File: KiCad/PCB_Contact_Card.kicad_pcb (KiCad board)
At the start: 2 copper layers, 90 x 54 mm, 6 parts

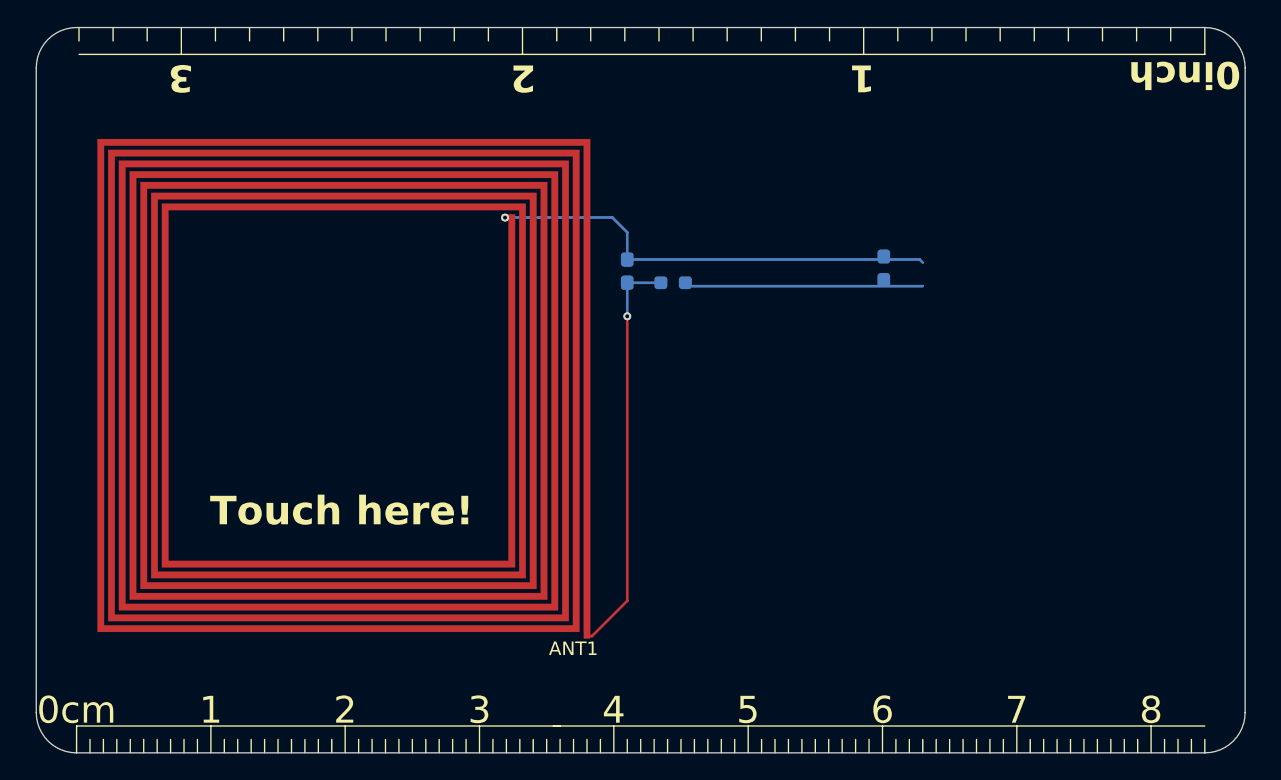
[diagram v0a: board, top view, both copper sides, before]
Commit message: footprint fixed
アンテナのフットプリントのバク修正
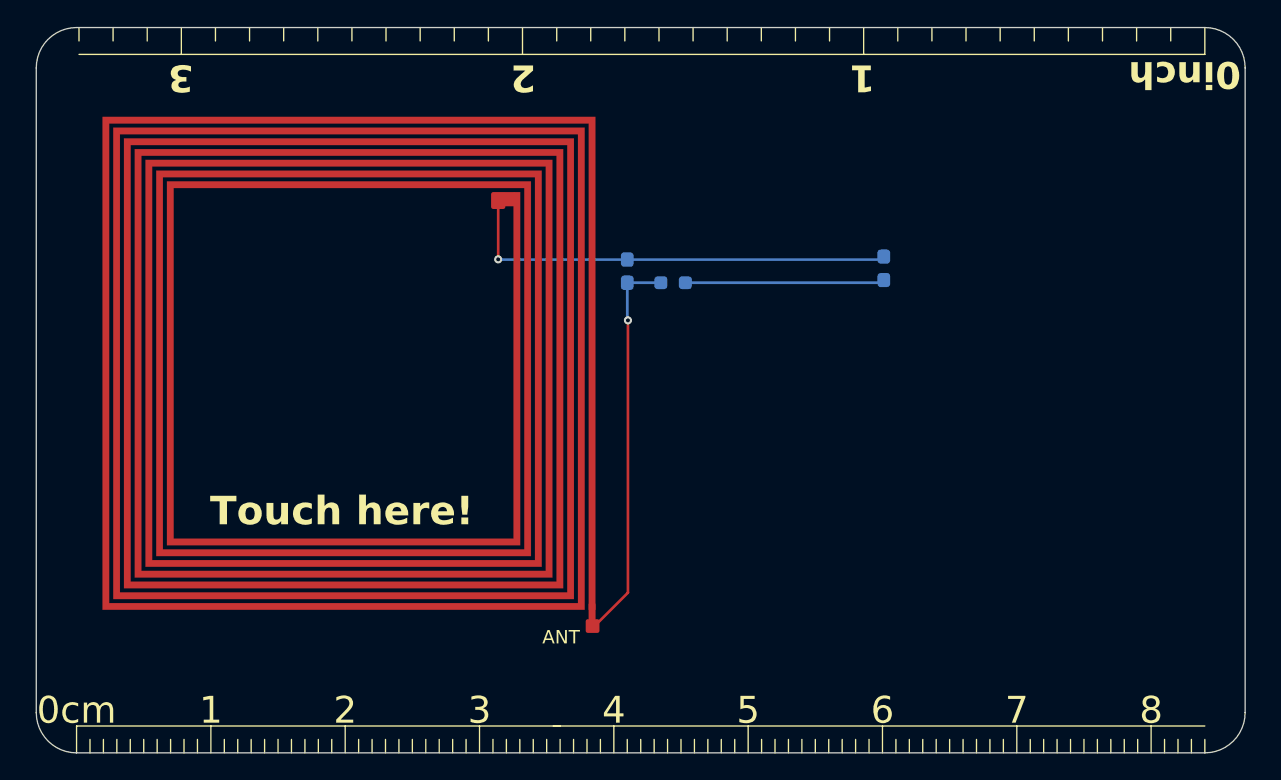
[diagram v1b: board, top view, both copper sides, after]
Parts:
- removed ANT1: L, PCB_BusinessCard_lib:NFC_COIL_36.7x36.7_3uH
- added ANT: L, lib:NFC_COIL_36.7x36.7_3uH, F.Cu at (116.6, 85.8)
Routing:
- net Net-(D1-A): track 17.8 -> 15.2 mm
- net Net-(C1-Pad2): track 30.3 -> 29.3 mm
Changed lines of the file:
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@@
 	(net 1 "Net-(D1-A)")
 	(net 2 "Net-(D1-K)")
-	(net 3 "Net-(ANT1-Pad1)")
-	(footprint "PCB_BusinessCard_lib:NFC_COIL_36.7x36.7_3uH"
+	(net 3 "Net-(C1-Pad2)")
+	(footprint "lib:NFC_COIL_36.7x36.7_3uH"
 		(layer "F.Cu")
-		(at 116.25 87.5 90)
-		(property "Reference" "ANT1"
-			(at -1.25 -1.25 0)
+		(at 116.63 85.85 90)
+		(property "Reference" "ANT"
+			(at -2.04 -2.56 0)
 			(unlocked yes)
 			(layer "F.SilkS")
@@
 		)
 		(property "Value" "L"
-			(at 0 1 90)
+			(at -0.07 1.55 90)
 			(unlocked yes)
 			(layer "F.Fab")
@@
 		(property ki_fp_filters "Choke_* *Coil* Inductor_* L_*")
 		(sheetname "/")
-		(sheetfile "PCB_BusinessCard.kicad_sch")
+		(sheetfile "PCB_Contact_Card.kicad_sch")
 		(attr smd)
+		(fp_rect
+			(start 30.14 -6.795)
+			(end 31 -6.105)
+			(stroke
+				(width 0.2)
+				(type solid)
+			)
+			(fill yes)
+			(layer "F.Cu")
+		)
+		(fp_rect
+			(start -0.67 -0.41)
+			(end 0.41 -0.09)
+			(stroke
+				(width 0.2)
+				(type solid)
+			)
+			(fill yes)
+			(layer "F.Cu")
+		)
 		(fp_poly
 			(pts
@@
 				(xy 2.4 -34.3) (xy 2.4 -3.2) (xy 33.5 -3.2) (xy 33.5 -33.5) (xy 3.2 -33.5) (xy 3.2 -4) (xy 32.7 -4)
 				(xy 32.7 -32.7) (xy 4 -32.7) (xy 4 -4.8) (xy 31.9 -4.8) (xy 31.9 -31.9) (xy 4.8 -31.9) (xy 4.8 -5.6)
-				(xy 31.1 -5.6) (xy 31.1 -6.1) (xy 30.6 -6.1) (xy 5.3 -6.1) (xy 5.3 -31.4) (xy 31.4 -31.4) (xy 31.4 -5.3)
+				(xy 31.1 -5.6) (xy 31.1 -6.1) (xy 30 -6.1) (xy 5.3 -6.1) (xy 5.3 -31.4) (xy 31.4 -31.4) (xy 31.4 -5.3)
 				(xy 4.5 -5.3) (xy 4.5 -32.2) (xy 32.2 -32.2) (xy 32.2 -4.5) (xy 3.7 -4.5) (xy 3.7 -33) (xy 33 -33)
 				(xy 33 -3.7) (xy 2.9 -3.7) (xy 2.9 -33.8) (xy 33.8 -33.8) (xy 33.8 -2.9) (xy 2.1 -2.9) (xy 2.1 -34.6)
@@
 			(layer "F.CrtYd")
 		)
-		(pad "1" smd rect
-			(at -0.25 -0.25 90)
-			(size 0.5 0.5)
+		(pad "1" smd roundrect
+			(at 30.470625 -7.23875 90)
+			(size 1.26125 1.0625)
 			(layers "F.Cu" "F.Mask" "F.Paste")
-			(net 3 "Net-(ANT1-Pad1)")
+			(roundrect_rratio 0.15)
+			(net 2 "Net-(D1-K)")
 			(pinfunction "1")
 			(pintype "passive")
-			(thermal_bridge_angle 45)
 		)
-		(pad "2" smd rect
-			(at 30.85 -6.35 90)
-			(size 0.5 0.5)
+		(pad "2" smd roundrect
+			(at -1.20875 -0.2125 90)
+			(size 1.0225 1.025)
 			(layers "F.Cu" "F.Mask" "F.Paste")
-			(net 2 "Net-(D1-K)")
+			(roundrect_rratio 0.15)
+			(net 3 "Net-(C1-Pad2)")
 			(pinfunction "2")
 			(pintype "passive")
-			(thermal_bridge_angle 45)
 		)
 		(embedded_fonts no)
@@
 		(property ki_fp_filters "C_*")
 		(sheetname "/")
-		(sheetfile "PCB_BusinessCard.kicad_sch")
+		(sheetfile "PCB_Contact_Card.kicad_sch")
 		(attr smd)
 		(fp_line
@@
 			(layers "B.Cu" "B.Mask" "B.Paste")
 			(roundrect_rratio 0.25)
-			(net 3 "Net-(ANT1-Pad1)")
+			(net 3 "Net-(C1-Pad2)")
 			(pintype "passive")
 		)
@@
 		(property ki_fp_filters "R_*")
 		(sheetname "/")
-		(sheetfile "PCB_BusinessCard.kicad_sch")
+		(sheetfile "PCB_Contact_Card.kicad_sch")
 		(attr smd)
 		(fp_line
@@
 			(layers "B.Cu" "B.Mask" "B.Paste")
 			(roundrect_rratio 0.25)
-			(net 3 "Net-(ANT1-Pad1)")
+			(net 3 "Net-(C1-Pad2)")
 			(pintype "passive")
 		)
@@
 		(property ki_fp_filters "LED* LED_SMD:* LED_THT:*")
 		(sheetname "/")
-		(sheetfile "PCB_BusinessCard.kicad_sch")
+		(sheetfile "PCB_Contact_Card.kicad_sch")
 		(attr smd)
 		(fp_line
@@
 	)
 	(segment
-		(start 141 61.75)
-		(end 123.575 61.75)
+		(start 123.325 61.5)
+		(end 137.9 61.5)
 		(width 0.2)
 		(layer "B.Cu")
 		(net 1)
 	)
-	(via
-		(at 109.9 56.65)
-		(size 0.6)
-		(drill 0.3)
-		(layers "F.Cu" "B.Cu")
+	(segment
+		(start 137.9 61.5)
+		(end 138.1 61.3)
+		(width 0.2)
+		(layer "B.Cu")
+		(net 1)
+	)
+	(segment
+		(start 109.39125 55.379375)
+		(end 109.39125 59.75875)
+		(width 0.2)
+		(layer "F.Cu")
 		(net 2)
 	)
 	(segment
-		(start 117.9 56.65)
-		(end 109.9 56.65)
+		(start 109.39125 59.75875)
+		(end 109.39 59.76)
 		(width 0.2)
-		(layer "B.Cu")
+		(layer "F.Cu")
+		(net 2)
+	)
+	(via
+		(at 109.39 59.76)
+		(size 0.6)
+		(drill 0.3)
+		(layers "F.Cu" "B.Cu")
 		(net 2)
 	)
 	(segment
-		(start 119 59.775)
-		(end 119 57.75)
+		(start 137.875 59.775)
+		(end 138.1 59.55)
 		(width 0.2)
 		(layer "B.Cu")
@@
 	(segment
 		(start 119 59.775)
-		(end 140.775 59.775)
+		(end 137.875 59.775)
 		(width 0.2)
 		(layer "B.Cu")
@@
 	)
 	(segment
-		(start 119 57.75)
-		(end 117.9 56.65)
+		(start 109.39 59.76)
+		(end 109.405 59.775)
 		(width 0.2)
 		(layer "B.Cu")
@@
 	)
 	(segment
-		(start 140.775 59.775)
-		(end 141 60)
+		(start 109.405 59.775)
+		(end 119 59.775)
 		(width 0.2)
 		(layer "B.Cu")
@@
 	)
 	(segment
-		(start 116.376749 87.806)
-		(end 116 87.806)
+		(start 119.05 84.5771)
+		(end 116.56835 87.05875)
 		(width 0.2)
 		(layer "F.Cu")
@@
 	)
 	(segment
-		(start 119 64)
-		(end 119 85.182749)
+		(start 119.05 64.3)
+		(end 119.05 84.5771)
 		(width 0.2)
 		(layer "F.Cu")
@@
 	)
 	(segment
-		(start 119 85.182749)
-		(end 116.376749 87.806)
+		(start 116.56835 87.05875)
+		(end 116.4175 87.05875)
 		(width 0.2)
 		(layer "F.Cu")
@@
 	)
 	(via
-		(at 119 64)
+		(at 119.05 64.3)
 		(size 0.6)
 		(drill 0.3)
@@
 	(segment
 		(start 119 61.5)
-		(end 119 64)
+		(end 119 64.25)
+		(width 0.2)
+		(layer "B.Cu")
+		(net 3)
+	)
+	(segment
+		(start 119 64.25)
+		(end 119.05 64.3)
 		(width 0.2)
 		(layer "B.Cu")
